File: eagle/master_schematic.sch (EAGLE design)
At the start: 107 parts

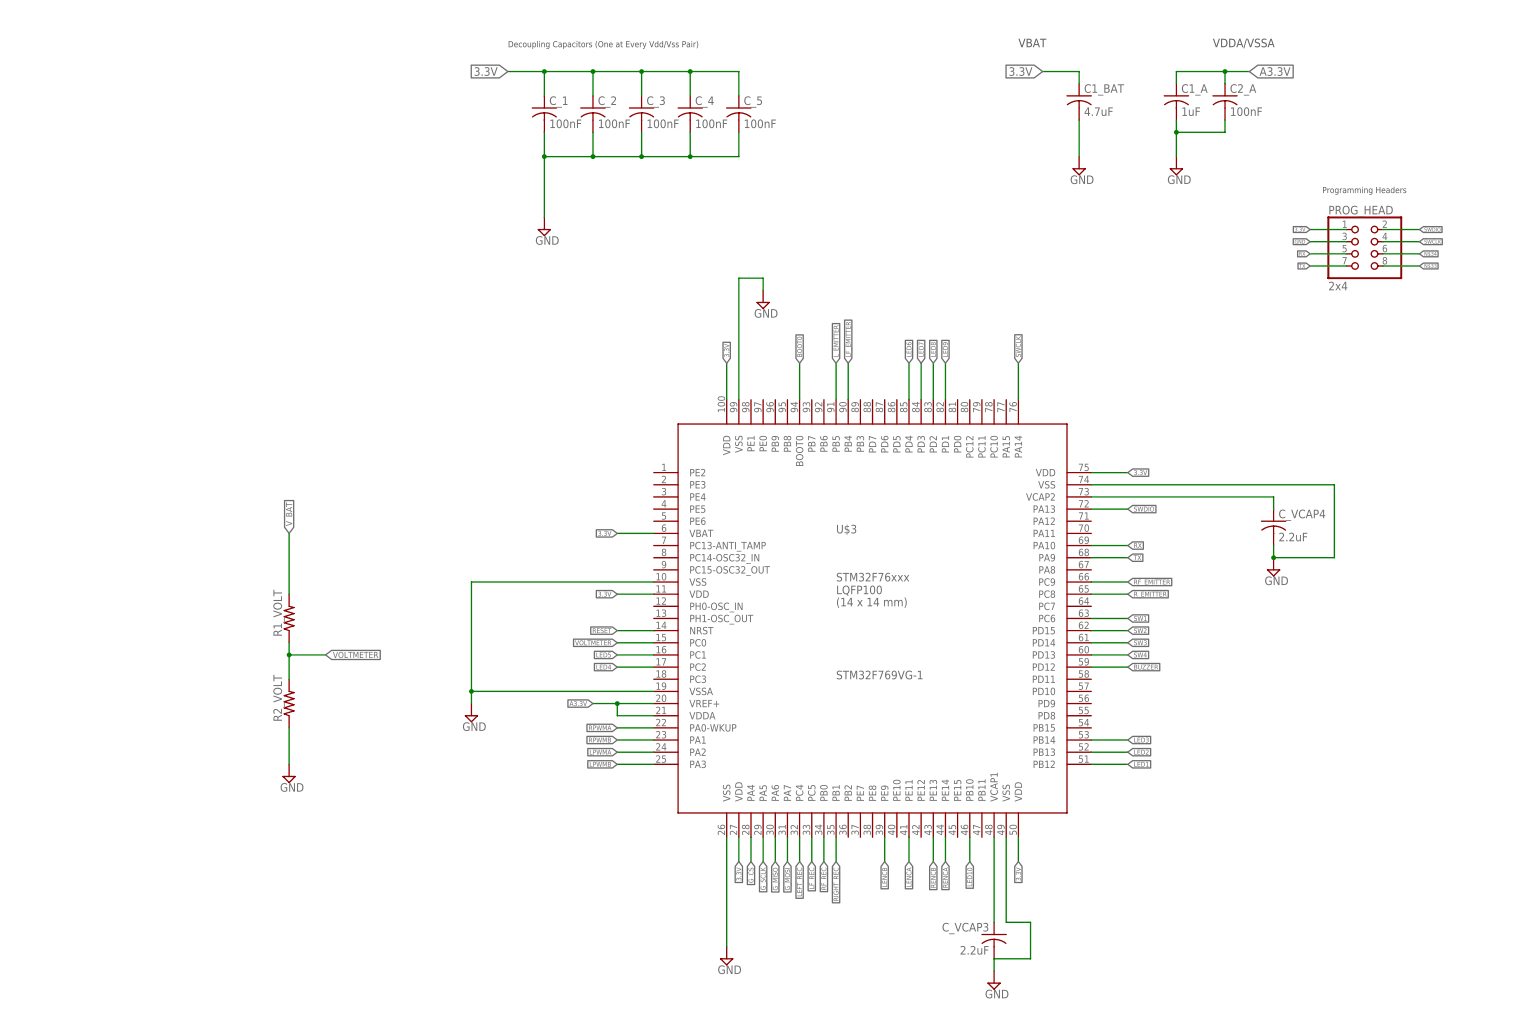
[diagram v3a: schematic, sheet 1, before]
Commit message: Delete Board
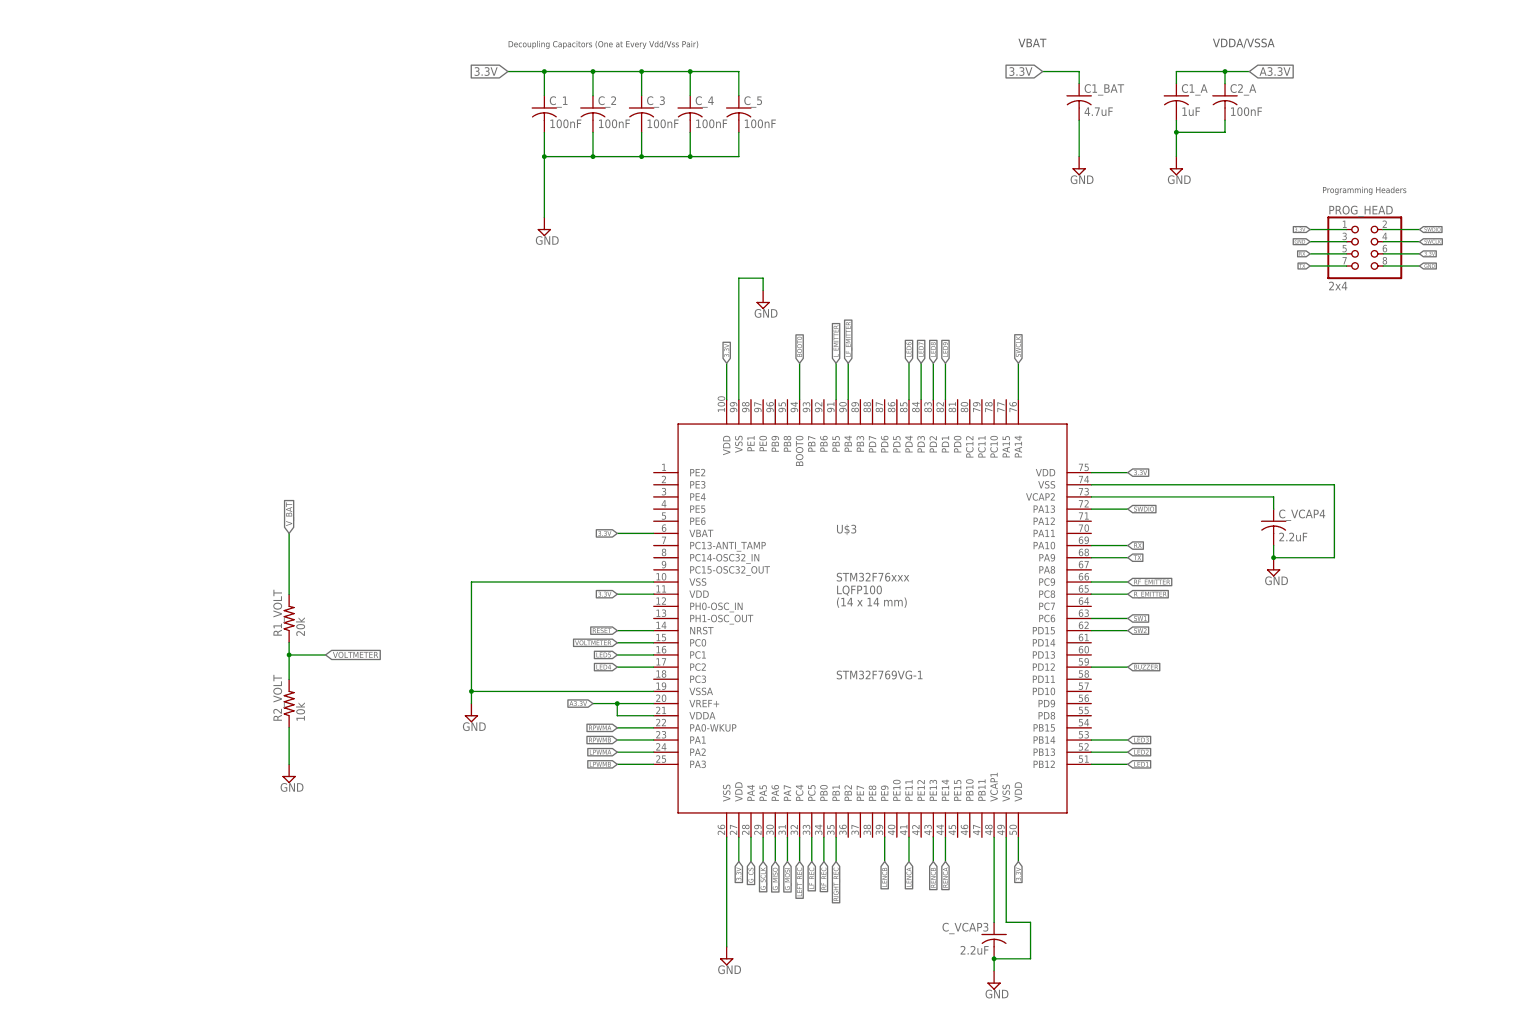
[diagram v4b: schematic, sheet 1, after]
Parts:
- R1_VOLT: value (none) -> 20k
- R2_VOLT: value (none) -> 10k
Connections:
- removed net LED10: U$3.PB10
- removed net N$33: PROG_HEAD.8
- removed net N$34: PROG_HEAD.6
- removed net SW3: U$3.PD14
- removed net SW4: U$3.PD13
- net 3.3V: now also PROG_HEAD.6
- net GND: now also PROG_HEAD.8
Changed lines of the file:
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@@
 <part name="SPK1" library="SMT-0540-S-R" deviceset="SMT-0540-S-R" device=""/>
 <part name="D2" library="diode" deviceset="DIODE-" device="SOD123" value="25V"/>
-<part name="R1_VOLT" library="resistor" deviceset="R-US_" device="R0805"/>
-<part name="R2_VOLT" library="resistor" deviceset="R-US_" device="R0805"/>
+<part name="R1_VOLT" library="resistor" deviceset="R-US_" device="R0805" value="20k"/>
+<part name="R2_VOLT" library="resistor" deviceset="R-US_" device="R0805" value="10k"/>
 <part name="SUPPLY3" library="supply2" deviceset="GND" device=""/>
 </parts>
@@
 <label x="-58.42" y="-27.94" size="1.016" layer="95" rot="R180" xref="yes"/>
 </segment>
+<segment>
+<pinref part="PROG_HEAD" gate="A" pin="6"/>
+<wire x1="101.6" y1="30.48" x2="109.22" y2="30.48" width="0.1524" layer="91"/>
+<label x="109.22" y="30.48" size="0.8128" layer="95" xref="yes"/>
+</segment>
 </net>
 <net name="A3.3V" class="0">
@@
 <wire x1="27.94" y1="-116.84" x2="20.32" y2="-116.84" width="0.1524" layer="91"/>
 <wire x1="20.32" y1="-116.84" x2="20.32" y2="-119.38" width="0.1524" layer="91"/>
+<junction x="20.32" y="-116.84"/>
 </segment>
 <segment>
@@
 <wire x1="-127" y1="-68.58" x2="-127" y2="-76.2" width="0.1524" layer="91"/>
 </segment>
+<segment>
+<pinref part="PROG_HEAD" gate="A" pin="8"/>
+<wire x1="101.6" y1="27.94" x2="109.22" y2="27.94" width="0.1524" layer="91"/>
+<label x="109.22" y="27.94" size="0.8128" layer="95" xref="yes"/>
+</segment>
 </net>
 <net name="BOOT0" class="0">
@@
 <wire x1="40.64" y1="-33.02" x2="48.26" y2="-33.02" width="0.1524" layer="91"/>
 <label x="48.26" y="-33.02" size="1.016" layer="95" xref="yes"/>
-</segment>
-</net>
-<net name="N$33" class="0">
-<segment>
-<pinref part="PROG_HEAD" gate="A" pin="8"/>
-<wire x1="101.6" y1="27.94" x2="109.22" y2="27.94" width="0.1524" layer="91"/>
-<label x="109.22" y="27.94" size="0.8128" layer="95" xref="yes"/>
-</segment>
-</net>
-<net name="N$34" class="0">
-<segment>
-<pinref part="PROG_HEAD" gate="A" pin="6"/>
-<wire x1="101.6" y1="30.48" x2="109.22" y2="30.48" width="0.1524" layer="91"/>
-<label x="109.22" y="30.48" size="0.8128" layer="95" xref="yes"/>
 </segment>
 </net>
@@
 </segment>
 </net>
-<net name="LED10" class="0">
-<segment>
-<pinref part="U$3" gate="G$1" pin="PB10"/>
-<wire x1="15.24" y1="-91.44" x2="15.24" y2="-96.52" width="0.1524" layer="91"/>
-<label x="15.24" y="-96.52" size="1.016" layer="95" rot="R270" xref="yes"/>
-</segment>
-</net>
 <net name="LED1" class="0">
 <segment>
@@
 </segment>
 </net>
-<net name="SW4" class="0">
-<segment>
-<pinref part="U$3" gate="G$1" pin="PD13"/>
-<wire x1="40.64" y1="-53.34" x2="48.26" y2="-53.34" width="0.1524" layer="91"/>
-<label x="48.26" y="-53.34" size="1.016" layer="95" xref="yes"/>
-</segment>
-</net>
-<net name="SW3" class="0">
-<segment>
-<pinref part="U$3" gate="G$1" pin="PD14"/>
-<wire x1="40.64" y1="-50.8" x2="48.26" y2="-50.8" width="0.1524" layer="91"/>
-<label x="48.26" y="-50.8" size="1.016" layer="95" xref="yes"/>
-</segment>
-</net>

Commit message: Fixed Inductors
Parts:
- removed L1: 470uH, resistor:L-USL1812
- removed L_3.3V, L_5.0V: 10uH, resistor:L-USL1812
- added L2, L3: 10uH, EagleLibrary_Wuerth_Elektronik_eiSos_rev16a:WE-MI_0805
- added L4: 470uH, EagleLibrary_Wuerth_Elektronik_eiSos_rev16a:WE-MI_0805
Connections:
- net 3.3V: now also L2.1; no longer L_3.3V.1
- net 5V: now also L3.1; no longer L_5.0V.2
- net A3.3V: now also L2.2, L4.1; no longer L1.1, L_3.3V.2
- net A5.0V: now also L3.2; no longer L_5.0V.1
- net N$14: now also L4.2; no longer L1.2

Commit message: Motor and Battery Mount
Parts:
- added U$1: BAT, mounts:BAT
- added U$2, U$5: MOTOR, mounts:MOTOR
- renumbered C1 to C3_G, C2 to C2_G, C4 to C4_G, C5 to C1_G, C_L_L1 to C_LREC, C_L_R1 to C_RREC, C_RESET3 to C_S2, C_US_1 to C_S1
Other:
- note added: "Battery Mount"
- note added: "Motor Mounts"

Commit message: Stuff
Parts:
- removed BAT_1, BAT_2: JST_2mm, SparkFun-Connectors:JST_2MM_MALE
- removed LF_REC1, L_REC1, RF_REC1, R_REC1: BP103, opto-trans-siemens:BP103
- added LF_REC, L_REC, RF_REC, R_REC: RECEIVER, sfh4550 & teft4300:RECEIVER
- added U$7, U$8: JST_CONNECTOR_FEMALE, JST_CONNECTOR_FEMALE. through hole:JST_CONNECTOR_FEMALE
- BOOT0: value A_HIGH -> (none)
- LED1, LED2, LED3, LED4, LED5, LED6, LED7, LED8, LED9: value 0805 -> (none)
- L_MOT: value L1 -> (none)
- PROG_HEAD: value 2x4 -> (none)
- PWR_LED: value PWR_LED -> (none)
- RST, S2, S3: value A_LOW -> (none)
- R_MOT: value R1 -> (none)
- renumbered LED10 to PWR_LED
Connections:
- net A3.3V: now also LF_REC.C, L_REC.C, RF_REC.C, R_REC.C; no longer LF_REC1.C, L_REC1.C, RF_REC1.C, R_REC1.C
- net GND: now also U$8.-; no longer BAT_2.-
- net LEFT_REC: now also L_REC.E; no longer LF_REC1.E
- net LF_REC: now also LF_REC.E; no longer L_REC1.E
- net N$31: now also U$7.+; no longer BAT_1.+
- net N$9: now also U$7.-, U$8.+; no longer BAT_1.-, BAT_2.+
- net RF_REC: now also RF_REC.E; no longer R_REC1.E
- net RIGHT_REC: now also R_REC.E; no longer RF_REC1.E
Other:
- moved on the sheet: R_R_R1

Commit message: ULN and stuff
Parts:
- removed U$4: ULN2003APWR, MMULN:ULN2003APWR
- added U$9: ULN2003APWR, ULN2003APWR:ULN2003APWR
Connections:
- net BUZZER: now also U$9.1B; no longer U$4.1B
- net GND: now also U$9.GND; no longer U$4.E
- net LF_EMITTER: now also U$9.7B; no longer U$4.7B
- net L_EMITTER: now also U$9.5B, U$9.6B; no longer U$4.5B, U$4.6B
- net N$22: now also U$9.2C; no longer U$4.2C
- net N$24: now also U$9.3C, U$9.4C; no longer U$4.3C, U$4.4C
- net N$27: now also U$9.5C, U$9.6C; no longer U$4.5C, U$4.6C
- net N$29: now also U$9.1C; no longer U$4.1C
- net N$30: now also U$9.7C; no longer U$4.7C
- net RF_EMITTER: now also U$9.2B; no longer U$4.2B
- net R_EMITTER: now also U$9.3B, U$9.4B; no longer U$4.3B, U$4.4B
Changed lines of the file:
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@@
 <part name="C1_F_EMITS" library="resistor" deviceset="C-EU" device="C1206" value="4.7uF"/>
 <part name="C2_F_EMITS" library="resistor" deviceset="C-EU" device="C1206" value=".1uF"/>
-<part name="U$4" library="MMULN" deviceset="ULN2003APWR" device=""/>
 <part name="R_MOT" library="pinhead" deviceset="PINHD-2X3" device=""/>
 <part name="L_MOT" library="pinhead" deviceset="PINHD-2X3" device=""/>
@@
 <part name="U$7" library="JST_CONNECTOR_FEMALE. through hole" deviceset="JST_CONNECTOR_FEMALE" device=""/>
 <part name="U$8" library="JST_CONNECTOR_FEMALE. through hole" deviceset="JST_CONNECTOR_FEMALE" device=""/>
+<part name="U$9" library="ULN2003APWR" deviceset="ULN2003APWR" device=""/>
 </parts>
 <sheets>
@@
 <instance part="C1_F_EMITS" gate="G$1" x="147.32" y="27.94" rot="R180"/>
 <instance part="C2_F_EMITS" gate="G$1" x="165.1" y="27.94" rot="R180"/>
-<instance part="U$4" gate="G$1" x="-17.78" y="0"/>
 <instance part="SUPPLY10" gate="GND" x="81.28" y="-17.78"/>
 <instance part="SUPPLY11" gate="GND" x="-45.72" y="-33.02"/>
@@
 <instance part="SPK1" gate="G$1" x="-7.62" y="45.72"/>
 <instance part="D2" gate="G$1" x="-7.62" y="38.1" rot="R180"/>
+<instance part="U$9" gate="G$1" x="-17.78" y="-2.54"/>
 </instances>
 <busses>
@@
 <net name="RF_EMITTER" class="0">
 <segment>
-<wire x1="-45.72" y1="12.7" x2="-40.64" y2="12.7" width="0.1524" layer="91"/>
 <label x="-45.72" y="12.7" size="1.778" layer="95" rot="R180" xref="yes"/>
-<pinref part="U$4" gate="G$1" pin="2B"/>
+<pinref part="U$9" gate="G$1" pin="2B"/>
+<wire x1="-45.72" y1="12.7" x2="-30.48" y2="12.7" width="0.1524" layer="91"/>
 </segment>
 </net>
@@
 <wire x1="-40.64" y1="2.54" x2="-40.64" y2="7.62" width="0.1524" layer="91"/>
 <label x="-45.72" y="2.54" size="1.778" layer="95" rot="R180" xref="yes"/>
-<pinref part="U$4" gate="G$1" pin="3B"/>
-<pinref part="U$4" gate="G$1" pin="4B"/>
+<pinref part="U$9" gate="G$1" pin="3B"/>
+<wire x1="-40.64" y1="7.62" x2="-30.48" y2="7.62" width="0.1524" layer="91"/>
+<pinref part="U$9" gate="G$1" pin="4B"/>
+<wire x1="-40.64" y1="2.54" x2="-30.48" y2="2.54" width="0.1524" layer="91"/>
 <junction x="-40.64" y="2.54"/>
 </segment>
@@
 <wire x1="-40.64" y1="-7.62" x2="-40.64" y2="-2.54" width="0.1524" layer="91"/>
 <label x="-45.72" y="-7.62" size="1.778" layer="95" rot="R180" xref="yes"/>
-<pinref part="U$4" gate="G$1" pin="5B"/>
-<pinref part="U$4" gate="G$1" pin="6B"/>
+<pinref part="U$9" gate="G$1" pin="5B"/>
+<wire x1="-40.64" y1="-2.54" x2="-30.48" y2="-2.54" width="0.1524" layer="91"/>
+<pinref part="U$9" gate="G$1" pin="6B"/>
+<wire x1="-40.64" y1="-7.62" x2="-30.48" y2="-7.62" width="0.1524" layer="91"/>
 <junction x="-40.64" y="-7.62"/>
 </segment>
@@
 <net name="LF_EMITTER" class="0">
 <segment>
-<wire x1="-40.64" y1="-12.7" x2="-45.72" y2="-12.7" width="0.1524" layer="91"/>
 <label x="-45.72" y="-12.7" size="1.778" layer="95" rot="R180" xref="yes"/>
-<pinref part="U$4" gate="G$1" pin="7B"/>
+<pinref part="U$9" gate="G$1" pin="7B"/>
+<wire x1="-45.72" y1="-12.7" x2="-30.48" y2="-12.7" width="0.1524" layer="91"/>
 </segment>
 </net>
@@
 <pinref part="R_RF" gate="G$1" pin="1"/>
 <junction x="12.7" y="12.7"/>
-<wire x1="12.7" y1="12.7" x2="5.08" y2="12.7" width="0.1524" layer="91"/>
-<pinref part="U$4" gate="G$1" pin="2C"/>
+<pinref part="U$9" gate="G$1" pin="2C"/>
+<wire x1="12.7" y1="12.7" x2="-5.08" y2="12.7" width="0.1524" layer="91"/>
 </segment>
 </net>
@@
 <wire x1="5.08" y1="7.62" x2="5.08" y2="2.54" width="0.1524" layer="91"/>
 <wire x1="17.78" y1="2.54" x2="5.08" y2="2.54" width="0.1524" layer="91"/>
-<pinref part="U$4" gate="G$1" pin="4C"/>
+<pinref part="U$9" gate="G$1" pin="4C"/>
+<wire x1="5.08" y1="2.54" x2="-5.08" y2="2.54" width="0.1524" layer="91"/>
 <junction x="5.08" y="2.54"/>
-<pinref part="U$4" gate="G$1" pin="3C"/>
+<pinref part="U$9" gate="G$1" pin="3C"/>
+<wire x1="5.08" y1="7.62" x2="-5.08" y2="7.62" width="0.1524" layer="91"/>
 </segment>
 </net>
@@
 <wire x1="5.08" y1="-2.54" x2="5.08" y2="-7.62" width="0.1524" layer="91"/>
 <wire x1="25.4" y1="-7.62" x2="5.08" y2="-7.62" width="0.1524" layer="91"/>
-<pinref part="U$4" gate="G$1" pin="6C"/>
+<pinref part="U$9" gate="G$1" pin="5C"/>
+<wire x1="5.08" y1="-2.54" x2="-5.08" y2="-2.54" width="0.1524" layer="91"/>
+<pinref part="U$9" gate="G$1" pin="6C"/>
+<wire x1="5.08" y1="-7.62" x2="-5.08" y2="-7.62" width="0.1524" layer="91"/>
 <junction x="5.08" y="-7.62"/>
-<pinref part="U$4" gate="G$1" pin="5C"/>
 </segment>
 </net>
@@
 <pinref part="R_LF" gate="G$1" pin="1"/>
 <junction x="38.1" y="-12.7"/>
-<wire x1="38.1" y1="-12.7" x2="5.08" y2="-12.7" width="0.1524" layer="91"/>
-<pinref part="U$4" gate="G$1" pin="7C"/>
+<wire x1="38.1" y1="-12.7" x2="-5.08" y2="-12.7" width="0.1524" layer="91"/>
+<pinref part="U$9" gate="G$1" pin="7C"/>
 </segment>
 </net>
 <net name="GND" class="0">
 <segment>
-<wire x1="-40.64" y1="-17.78" x2="-45.72" y2="-17.78" width="0.1524" layer="91"/>
 <wire x1="-45.72" y1="-17.78" x2="-45.72" y2="-30.48" width="0.1524" layer="91"/>
-<pinref part="U$4" gate="G$1" pin="E"/>
 <pinref part="SUPPLY11" gate="GND" pin="GND"/>
+<pinref part="U$9" gate="G$1" pin="GND"/>
+<wire x1="-45.72" y1="-17.78" x2="-30.48" y2="-17.78" width="0.1524" layer="91"/>
 </segment>
 <segment>
@@
 <net name="BUZZER" class="0">
 <segment>
-<pinref part="U$4" gate="G$1" pin="1B"/>
-<wire x1="-40.64" y1="17.78" x2="-45.72" y2="17.78" width="0.1524" layer="91"/>
 <label x="-45.72" y="17.78" size="1.778" layer="95" rot="R180" xref="yes"/>
+<pinref part="U$9" gate="G$1" pin="1B"/>
+<wire x1="-45.72" y1="17.78" x2="-30.48" y2="17.78" width="0.1524" layer="91"/>
 </segment>
 </net>
 <net name="N$29" class="0">
 <segment>
-<pinref part="U$4" gate="G$1" pin="1C"/>
-<wire x1="7.62" y1="17.78" x2="5.08" y2="17.78" width="0.1524" layer="91"/>
 <pinref part="SPK1" gate="G$1" pin="-"/>
 <wire x1="-2.54" y1="45.72" x2="7.62" y2="45.72" width="0.1524" layer="91"/>
@@
 <wire x1="-5.08" y1="38.1" x2="7.62" y2="38.1" width="0.1524" layer="91"/>
 <junction x="7.62" y="38.1"/>
-</segment>
-</net>
+<pinref part="U$9" gate="G$1" pin="1C"/>
+<wire x1="7.62" y1="17.78" x2="-5.08" y2="17.78" width="0.1524" layer="91"/>
+</segment>
+</net>
